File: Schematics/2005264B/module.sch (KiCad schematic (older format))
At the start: 0 parts

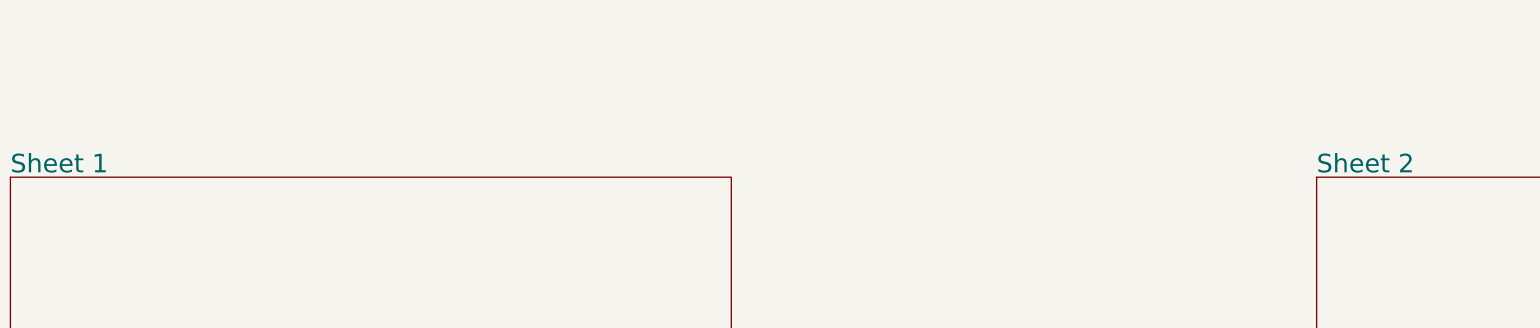
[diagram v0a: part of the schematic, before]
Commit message: Cross-checked/corrected module A14's 2005264A and 2005264B drawings vs pin database.  Predecessor drawings (2005264- etc.) not yet corrected.
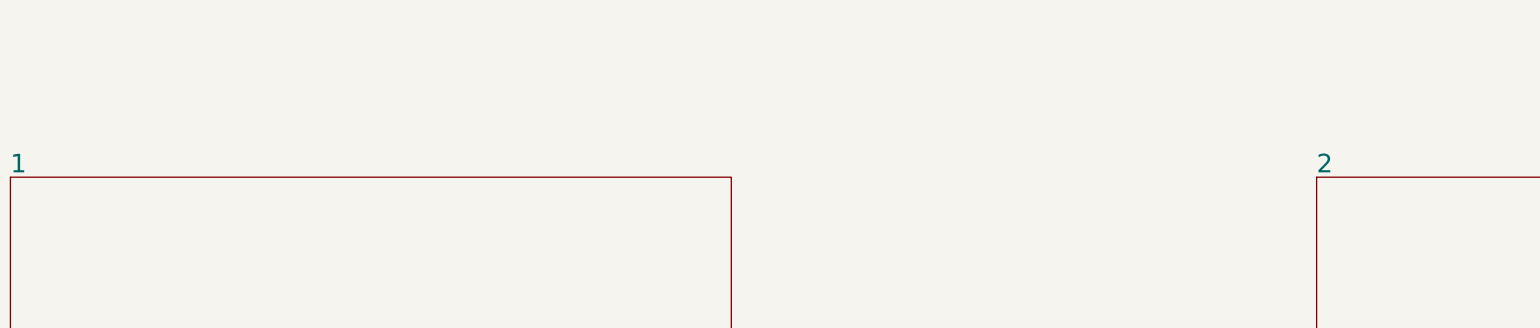
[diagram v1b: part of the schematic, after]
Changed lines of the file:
@@
 S 15250 11550 5450 8975
 U 5B8E7731
-F0 "Sheet 1" 140
+F0 "1" 140
 F1 "2005264B-p1of2.sch" 140
 F2 "0VDCA" U R 20700 17550 140
@@
 S 25125 11550 5450 8975
 U 5B8E7796
-F0 "Sheet 2" 140
+F0 "2" 140
 F1 "2005264B-p2of2.sch" 140
 F2 "0VDCA" U L 25125 17550 140
